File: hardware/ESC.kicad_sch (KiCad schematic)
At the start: 85 parts, among them J1 +, J2 -, J3 +, J4 +, J5 +, J6 +, J7 Conn_01x03, J8 +, J9 +, Q1 AGM60P30AP, Q2 AGM60P30AP, Q3 AGM60P30AP, Q4 AGM60P30AP, Q5 AGM60P30AP, Q6 AGM60P30AP, Q7 AGM60P30A, U1 DRV8323RSRGZR, U2 STM32G431CBTx, Y1 X322516MLB4SI

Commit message: added boot button and reset pad
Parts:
- added J10: +, Connector_Wire:SolderWirePad_1x01_SMD_2x4mm, symbol Connector_Generic:Conn_01x01
- added R28: 10K, Resistor_SMD:R_0402_1005Metric, symbol Device:R
- added SW3: SW_Push, Button_Switch_SMD:SW_Push_SPST_NO_Alps_SKRK, symbol Switch:SW_Push
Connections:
- net +3.3V: now also SW3.1
- net FAULT: now also U2.43 (PB6)
- net GND: now also R28.2
- net BOOT: now reaches U2.45 (PB8)
- net BOOT: now also R28.1, SW3.2
- net RESET: now reaches U2.7 (PG10)
- net RESET: now also J10.1 (Pin_1)
- no-connect marks 10 -> 7

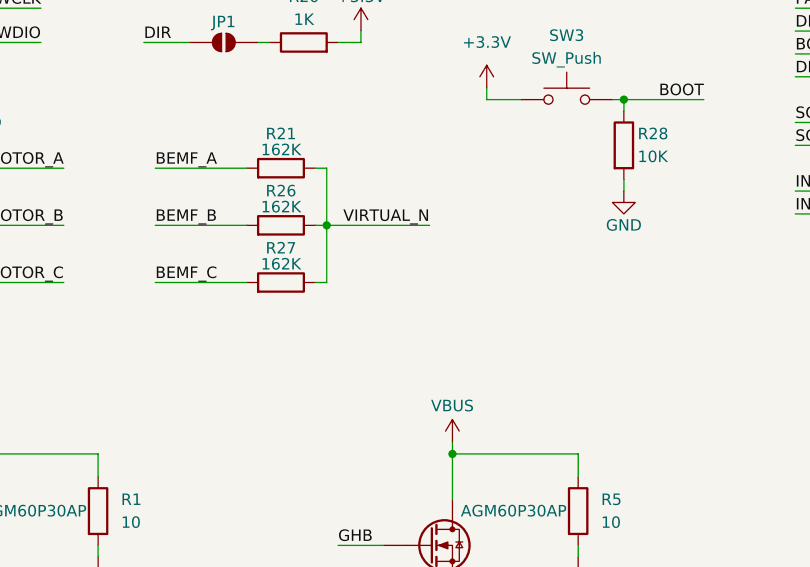
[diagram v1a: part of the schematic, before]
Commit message: added filter cap to virtual gnd
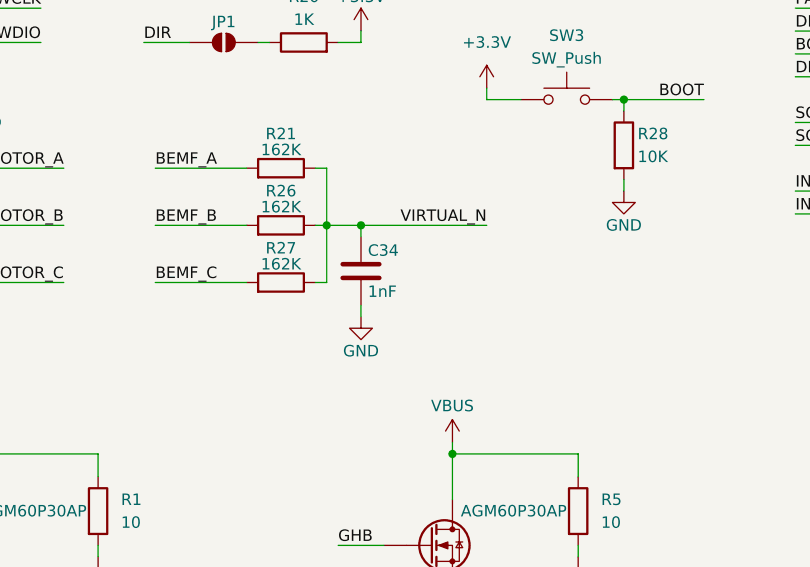
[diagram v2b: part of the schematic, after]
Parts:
- added C34: 1nF, Capacitor_SMD:C_0402_1005Metric, symbol Device:C
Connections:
- net GND: now also C34.2
- net VIRTUAL_N: now also C34.1
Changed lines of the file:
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@@
 	)
 	(junction
+		(at 71.12 109.22)
+		(diameter 0)
+		(color 0 0 0 0)
+	)
+	(junction
 		(at 260.35 63.5)
 		(diameter 0)
@@
 	(wire
 		(pts
+			(xy 71.12 118.11) (xy 71.12 119.38)
+		)
+		(stroke
+			(width 0)
+			(type default)
+		)
+	)
+	(wire
+		(pts
 			(xy 123.19 186.69) (xy 130.81 186.69)
 		)
@@
 	(wire
 		(pts
+			(xy 71.12 109.22) (xy 71.12 110.49)
+		)
+		(stroke
+			(width 0)
+			(type default)
+		)
+	)
+	(wire
+		(pts
 			(xy 15.24 144.78) (xy 20.32 144.78)
 		)
@@
 	(wire
 		(pts
+			(xy 71.12 109.22) (xy 85.09 109.22)
+		)
+		(stroke
+			(width 0)
+			(type default)
+		)
+	)
+	(wire
+		(pts
 			(xy 27.94 133.35) (xy 27.94 134.62)
 		)
@@
 	(wire
 		(pts
-			(xy 67.31 109.22) (xy 78.74 109.22)
+			(xy 67.31 109.22) (xy 71.12 109.22)
 		)
 		(stroke
@@
 	)
 	(label "VIRTUAL_N"
-		(at 78.74 109.22 180)
+		(at 85.09 109.22 180)
 		(effects
 			(font
@@
 	)
 	(symbol
+		(lib_id "power:GND")
+		(at 71.12 119.38 0)
+		(unit 1)
+		(body_style 1)
+		(exclude_from_sim no)
+		(in_bom yes)
+		(on_board yes)
+		(in_pos_files yes)
+		(dnp no)
+		(property "Reference" "#PWR054"
+			(at 71.12 125.73 0)
+			(hide yes)
+			(show_name no)
+			(do_not_autoplace no)
+			(effects
+				(font
+					(size 1.27 1.27)
+				)
+			)
+		)
+		(property "Value" "GND"
+			(at 71.12 123.19 0)
+			(show_name no)
+			(do_not_autoplace no)
+			(effects
+				(font
+					(size 1.27 1.27)
+				)
+			)
+		)
+		(property "Footprint" ""
+			(at 71.12 119.38 0)
+			(hide yes)
+			(show_name no)
+			(do_not_autoplace no)
+			(effects
+				(font
+					(size 1.27 1.27)
+				)
+			)
+		)
+		(property "Datasheet" ""
+			(at 71.12 119.38 0)
+			(hide yes)
+			(show_name no)
+			(do_not_autoplace no)
+			(effects
+				(font
+					(size 1.27 1.27)
+				)
+			)
+		)
+		(property "Description" "Power symbol creates a global label with name \"GND\" , ground"
+			(at 71.12 119.38 0)
+			(hide yes)
+			(show_name no)
+			(do_not_autoplace no)
+			(effects
+				(font
+					(size 1.27 1.27)
+				)
+			)
+		)
+		(pin "1"
+		)
+		(instances
+			(project "ESC"
+				(path "/4de1658d-a5e4-45f8-9b2f-349bf6ebe789"
+					(reference "#PWR054")
+					(unit 1)
+				)
+			)
+		)
+	)
+	(symbol
 		(lib_id "Device:R")
 		(at 190.5 66.04 90)
@@
 					(unit 1)
 				)
+			)
+		)
+	)
+	(symbol
+		(lib_id "Device:C")
+		(at 71.12 114.3 0)
+		(unit 1)
+		(body_style 1)
+		(exclude_from_sim no)
+		(in_bom yes)
+		(on_board yes)
+		(in_pos_files yes)
+		(dnp no)
+		(property "Reference" "C34"
+			(at 71.882 112.014 0)
+			(show_name no)
+			(do_not_autoplace no)
+			(effects
+				(font
+					(size 1.27 1.27)
+				)
+				(justify left)
+			)
+		)
+		(property "Value" "1nF"
+			(at 71.882 116.586 0)
+			(show_name no)
+			(do_not_autoplace no)
+			(effects
+				(font
+					(size 1.27 1.27)
+				)
+				(justify left)
+			)
+		)
+		(property "Footprint" "Capacitor_SMD:C_0402_1005Metric"
+			(at 72.0852 118.11 0)
+			(hide yes)
+			(show_name no)
+			(do_not_autoplace no)
+			(effects
+				(font
+					(size 1.27 1.27)
+				)
+			)
+		)
+		(property "Datasheet" ""
+			(at 71.12 114.3 0)
+			(hide yes)
+			(show_name no)
+			(do_not_autoplace no)
+			(effects
+				(font
+					(size 1.27 1.27)
+				)
+			)
+		)
+		(property "Description" "Unpolarized capacitor"
+			(at 71.12 114.3 0)
+			(hide yes)
+			(show_name no)
+			(do_not_autoplace no)
+			(effects
+				(font
+					(size 1.27 1.27)
+				)
+			)
+		)
+		(pin "1"
+		)
+		(pin "2"
+		)
+		(instances
+			(project "ESC"
+				(path "/4de1658d-a5e4-45f8-9b2f-349bf6ebe789"
+					(reference "C34")
+					(unit 1)
+				)

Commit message: changed inductor size
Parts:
- L1: footprint Inductor_SMD:L_APV_ANR5012 -> Inductor_SMD:L_APV_ANR6020
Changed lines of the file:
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@@
 			)
 		)
-		(property "Footprint" "Inductor_SMD:L_APV_ANR5012"
+		(property "Footprint" "Inductor_SMD:L_APV_ANR6020"
 			(at 266.7 66.04 0)
 			(hide yes)

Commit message: beautified schematic
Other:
- note added: "Bulk Capacitance"
- note added: "Direction Setting"
- note added: "Gate Driver"
- note added: "Headers"
- note added: "Microcontroller"
- note added: "Power Input"
- note added: "Switching MOSFETs"
- note added: "Virtual Ground"
- note added: "Voltage Monitor"
- moved on the sheet: C1, C10, C11, C12, C13, C14, C15, C16, C17, C18, C19, C2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

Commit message: added new single side design
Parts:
- added U3: LMR16006YQ, Package_TO_SOT_SMD:SOT-23-6, symbol Regulator_Switching:LMR16006YQ
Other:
- moved on the sheet: C10, C11, C12, C13, C14, C7, C8, C9, D1, FB1, L1, R10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

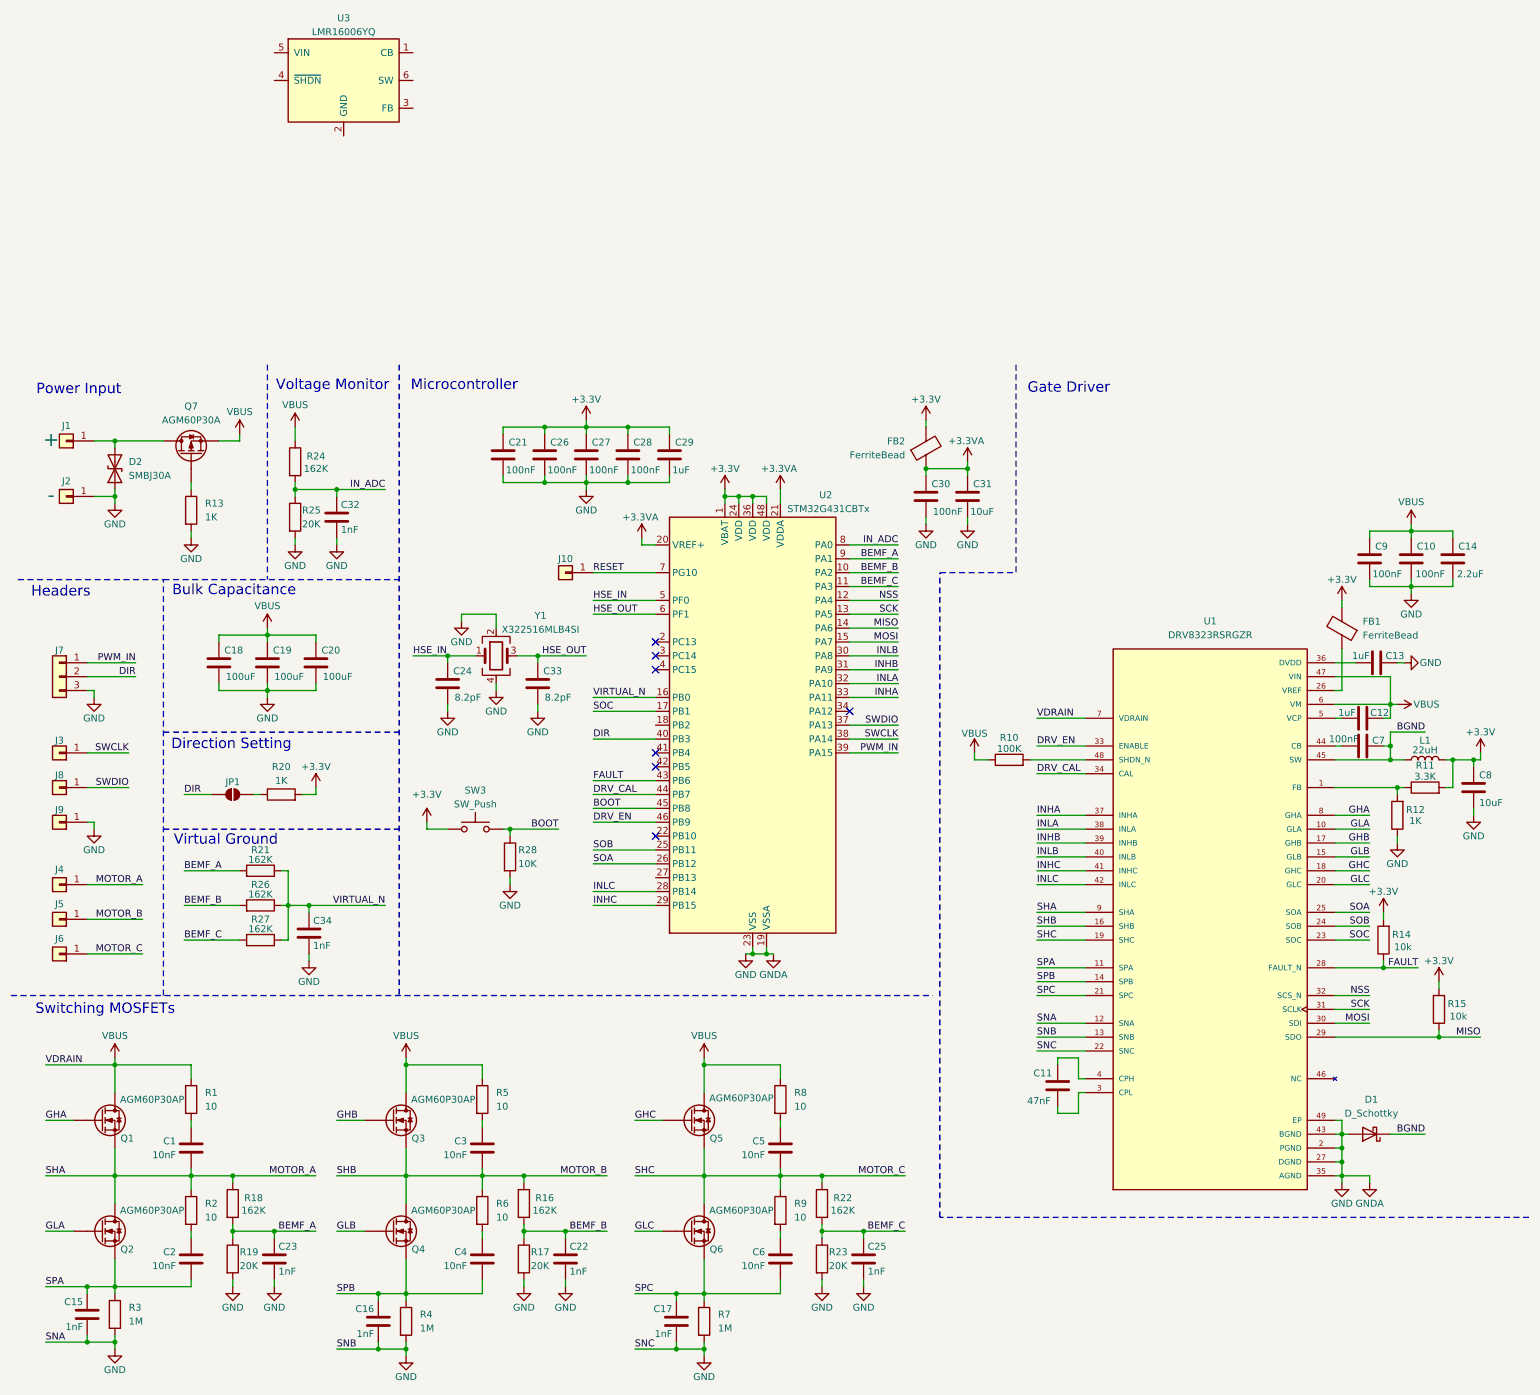
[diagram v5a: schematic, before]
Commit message: added new regulator and gate driver
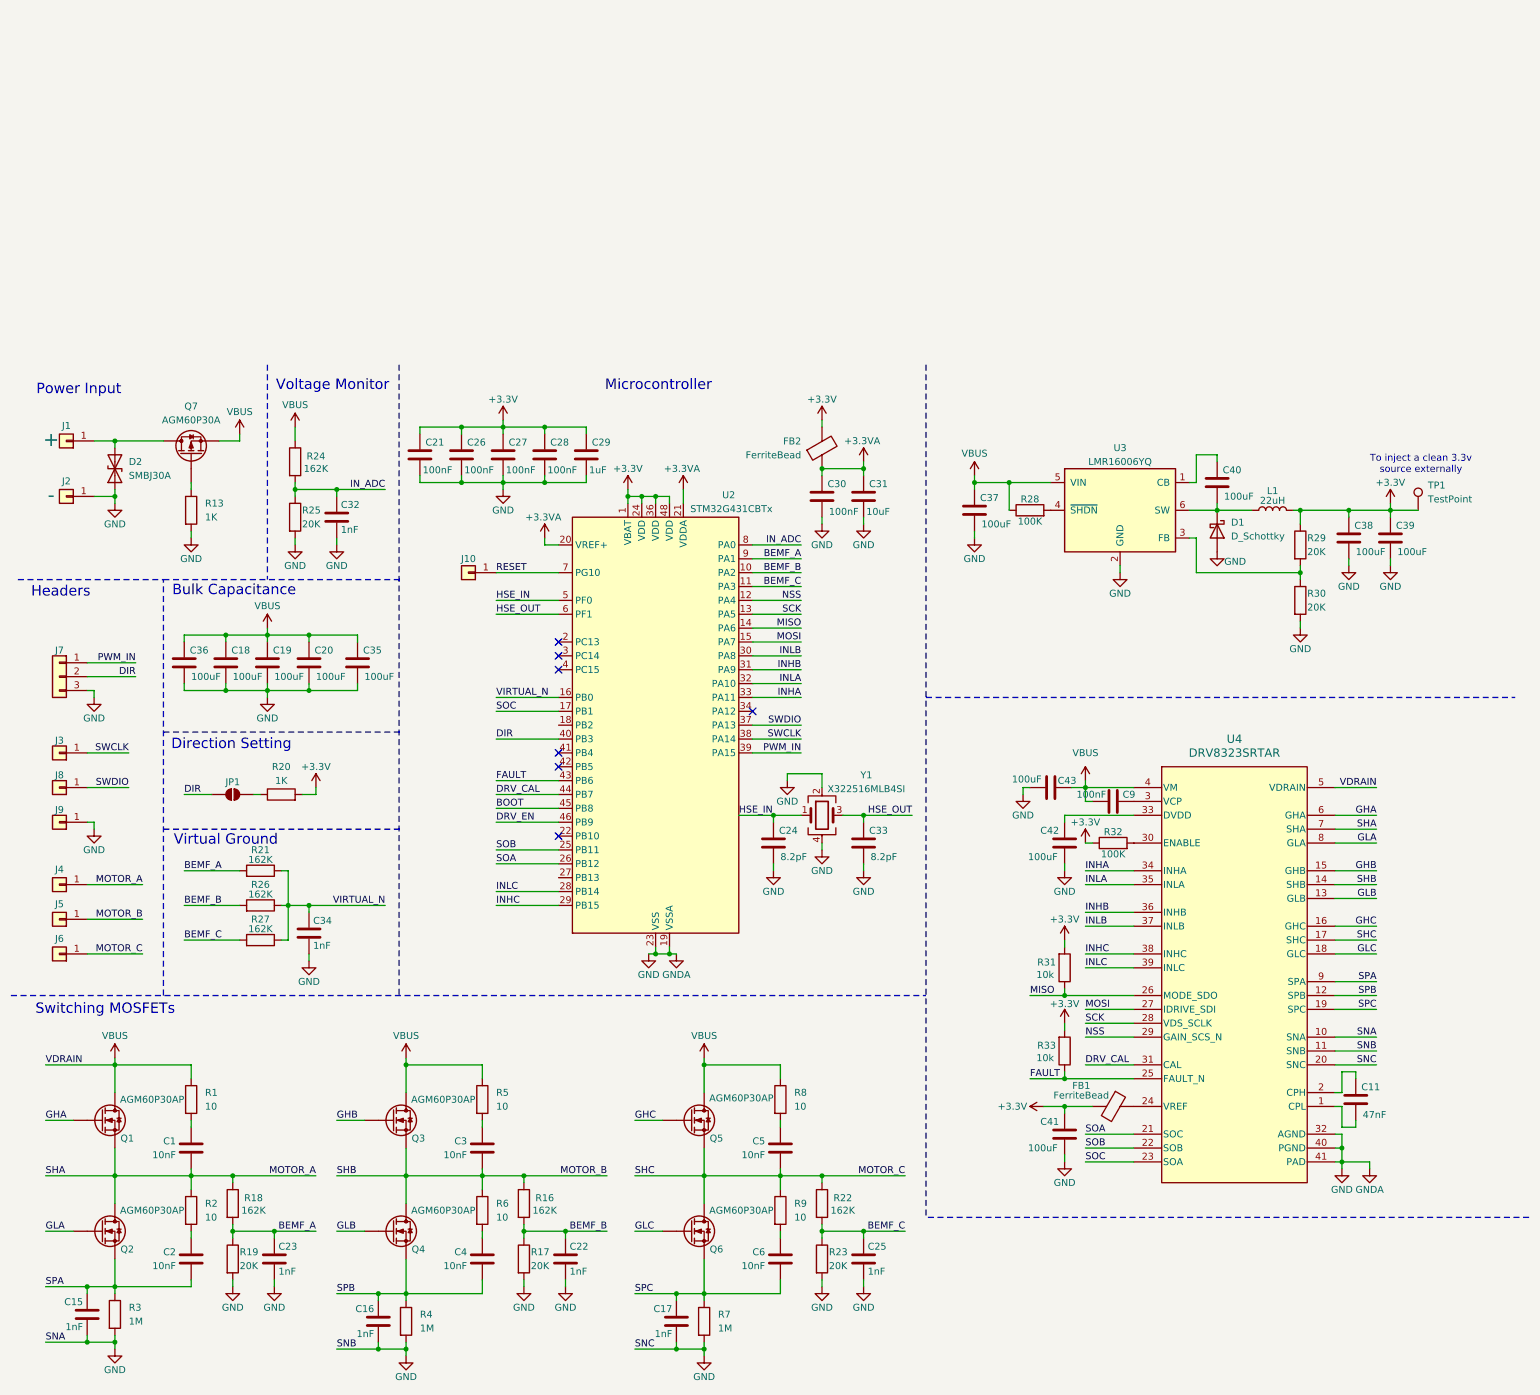
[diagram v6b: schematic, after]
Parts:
- removed C10, C7: 100nF, Capacitor_SMD:C_0402_1005Metric, symbol Device:C
- removed C12, C13: 1uF, Capacitor_SMD:C_0402_1005Metric, symbol Device:C
- removed C14: 2.2uF, Capacitor_SMD:C_0603_1608Metric, symbol Device:C
- removed C8: 10uF, Capacitor_SMD:C_0603_1608Metric, symbol Device:C
- removed R10: 100K, Resistor_SMD:R_0402_1005Metric, symbol Device:R
- removed R11: 3.3K, Resistor_SMD:R_0402_1005Metric, symbol Device:R
- removed R12: 1K, Resistor_SMD:R_0402_1005Metric, symbol Device:R
- removed R14, R15: 10k, Resistor_SMD:R_0402_1005Metric, symbol Device:R
- removed SW3: SW_Push, Button_Switch_SMD:SW_Push_SPST_NO_Alps_SKRK, symbol Switch:SW_Push
- removed U1: DRV8323RSRGZR, Package_DFN_QFN:QFN-48-1EP_7x7mm_P0.5mm_EP5.1x5.1mm_ThermalVias, symbol ESC-Imports:DRV8323RSRGZR
- added C35, C36, C37, C38, C39, C40, C41, C42, C43: 100uF, Capacitor_SMD:C_Elec_6.3x7.7, symbol Device:C
- added R29, R30: 20K, Resistor_SMD:R_0402_1005Metric, symbol Device:R
- added R31, R33: 10k, Resistor_SMD:R_0402_1005Metric, symbol Device:R
- added R32: 100K, Resistor_SMD:R_0402_1005Metric, symbol Device:R
- added TP1: TestPoint, TestPoint:TestPoint_Pad_1.5x1.5mm, symbol Connector:TestPoint
- added U4: DRV8323SRTAR, RTA0040B, symbol ESC-Imports:DRV8323SRTAR
- R28: value 10K -> 100K
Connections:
- net BGND is gone; now on an unnamed net: D1.1 (K), L1.1
- net +3.3V: now also C38.1, C39.1, C41.1, R29.1, R31.2, R32.1, R33.2, TP1.1
- net BOOT: no longer R28.1
- net DRV_CAL: now also U4.31 (CAL)
- net FAULT: now also R33.1, U4.25 (FAULT_N)
- net GHA: now also U4.6 (GHA)
- net GHB: now also U4.15 (GHB)
- net GHC: now also U4.16 (GHC)
- net GLA: now also U4.8 (GLA)
- net GLB: now also U4.13 (GLB)
- net GLC: now also U4.18 (GLC)
- net GND: now also U3.2 (GND), C35.2, C36.2, C37.2, C38.2, C39.2, C41.2, C42.2, C43.2, R30.2, U4.10 (SNA), U4.11 (SNB), U4.20 (SNC), U4.32 (AGND), U4.40 (PGND), U4.41 (PAD); no longer C9.2, R28.2
- net INHA: now also U4.34 (INHA)
- net INHB: now also U4.36 (INHB)
- net INHC: now also U4.38 (INHC)
- net INLA: now also U4.35 (INLA)
- net INLB: now also U4.37 (INLB)
- net INLC: now also U4.39 (INLC)
- net MISO: now also R31.1, U4.26 (MODE_SDO)
- net MOSI: now also U4.27 (IDRIVE_SDI)
- net MOTOR_A: now also U4.7 (SHA)
- net MOTOR_B: now also U4.14 (SHB)
- net MOTOR_C: now also U4.17 (SHC)
- net NSS: now also U4.29 (GAIN_SCS_N)
- net SCK: now also U4.28 (VDS_SCLK)
- net SOA: now also U4.21 (SOC)
- net SOB: now also U4.22 (SOB)
- net SOC: now also U4.23 (SOA)
- net SPA: now also U4.9 (SPA)
- net SPB: now also U4.12 (SPB)
- net SPC: now also U4.19 (SPC)
- net VBUS: now also R28.1, U3.5 (VIN), C35.1, C36.1, C37.1, C43.1, U4.4 (VM), U4.5 (VDRAIN)
- net at C11.1: now also U4.2 (CPH)
- net at C11.2: now also U4.1 (CPL)
- net at FB1.1: now also U4.24 (VREF)
- net at U3.1 (CB): now also C40.1
- net at U3.3 (FB): now also R29.2, R30.1
- net at U3.4 (~{SHDN}): now also R28.2
- net at U3.6 (SW): now also C40.2
- new net: R32.2, U4.30 (ENABLE)
- new net: C42.1, U4.33 (DVDD)
- new net: C9.2, U4.3 (VCP)
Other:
- note added: "To inject a clean 3.3v source externally"
- note removed: "Gate Driver"
- moved on the sheet: C18, C20, C21, C24, C26, C27, C28, C29, C30, C31, C33, FB2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

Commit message: added lables
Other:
- note added: "Buck Regulator"
- note added: "Gate Driver"
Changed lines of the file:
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@@
 	(generator_version "10.0")
 	(paper "A4")
+	(text "Buck Regulator"
+		(exclude_from_sim no)
+		(at 187.96 14.224 0)
+		(effects
+			(font
+				(size 1.905 1.905)
+			)
+		)
+	)
 	(text "Bulk Capacitance"
 		(exclude_from_sim no)
@@
 	(text "Microcontroller"
 		(exclude_from_sim no)
-		(at 127.508 13.97 0)
+		(at 91.44 13.97 0)
 		(effects
 			(font
@@
 		(effects
 			(font
+				(size 1.905 1.905)
+			)
+		)
+	)
+	(text "Gate Driver"
+		(exclude_from_sim no)
+		(at 187.706 73.406 0)
+		(effects
+			(font
